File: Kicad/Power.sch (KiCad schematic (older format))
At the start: 40 parts, among them J4 Conn_01x03, J5 Conn_01x04, K1 G5Q-1, K2 G5Q-1, Q6 BC547, T1 Transformer_1P_1S, T2 Transformer_1P_2S, U5 EL817, U6 L7805, U7 L7812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

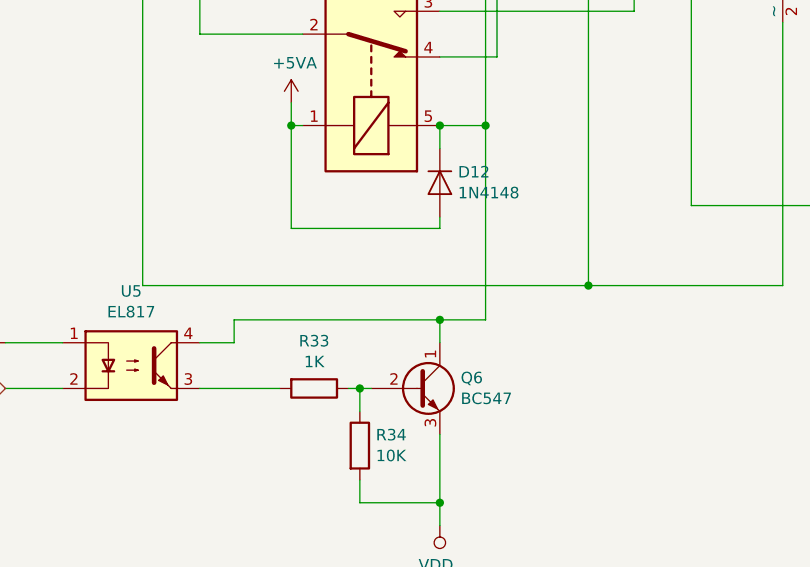
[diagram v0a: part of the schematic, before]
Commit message: fixed bugs in PCB, added frontpanel, added SW for frontpanel
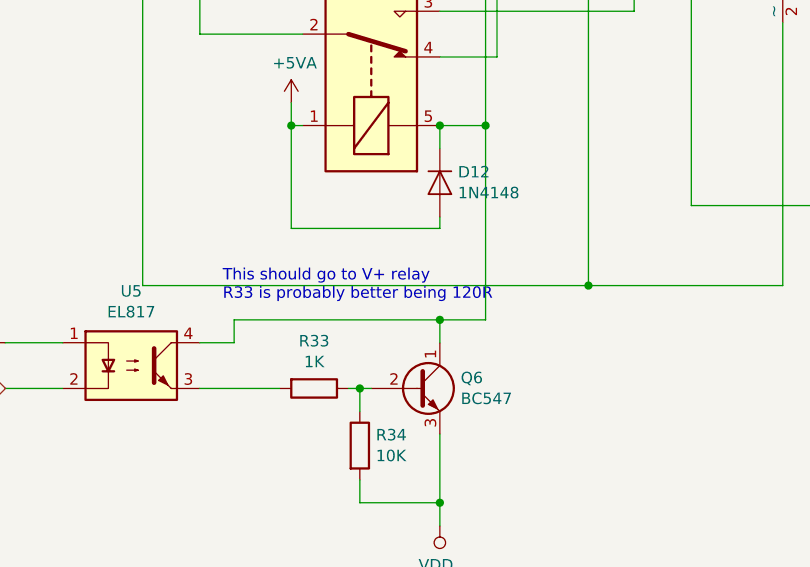
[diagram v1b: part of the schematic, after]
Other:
- note added: "This should go to V+ relay\nR33 is probably better being 120R\n\n"
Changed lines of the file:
@@
 	0    1    -1   0
 $EndComp
+Text Notes 4550 8300 0    50   ~ 0
+This should go to V+ relay\nR33 is probably better being 120R\n\n
 $EndSCHEMATC
